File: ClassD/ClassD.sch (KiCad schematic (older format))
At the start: 1 part

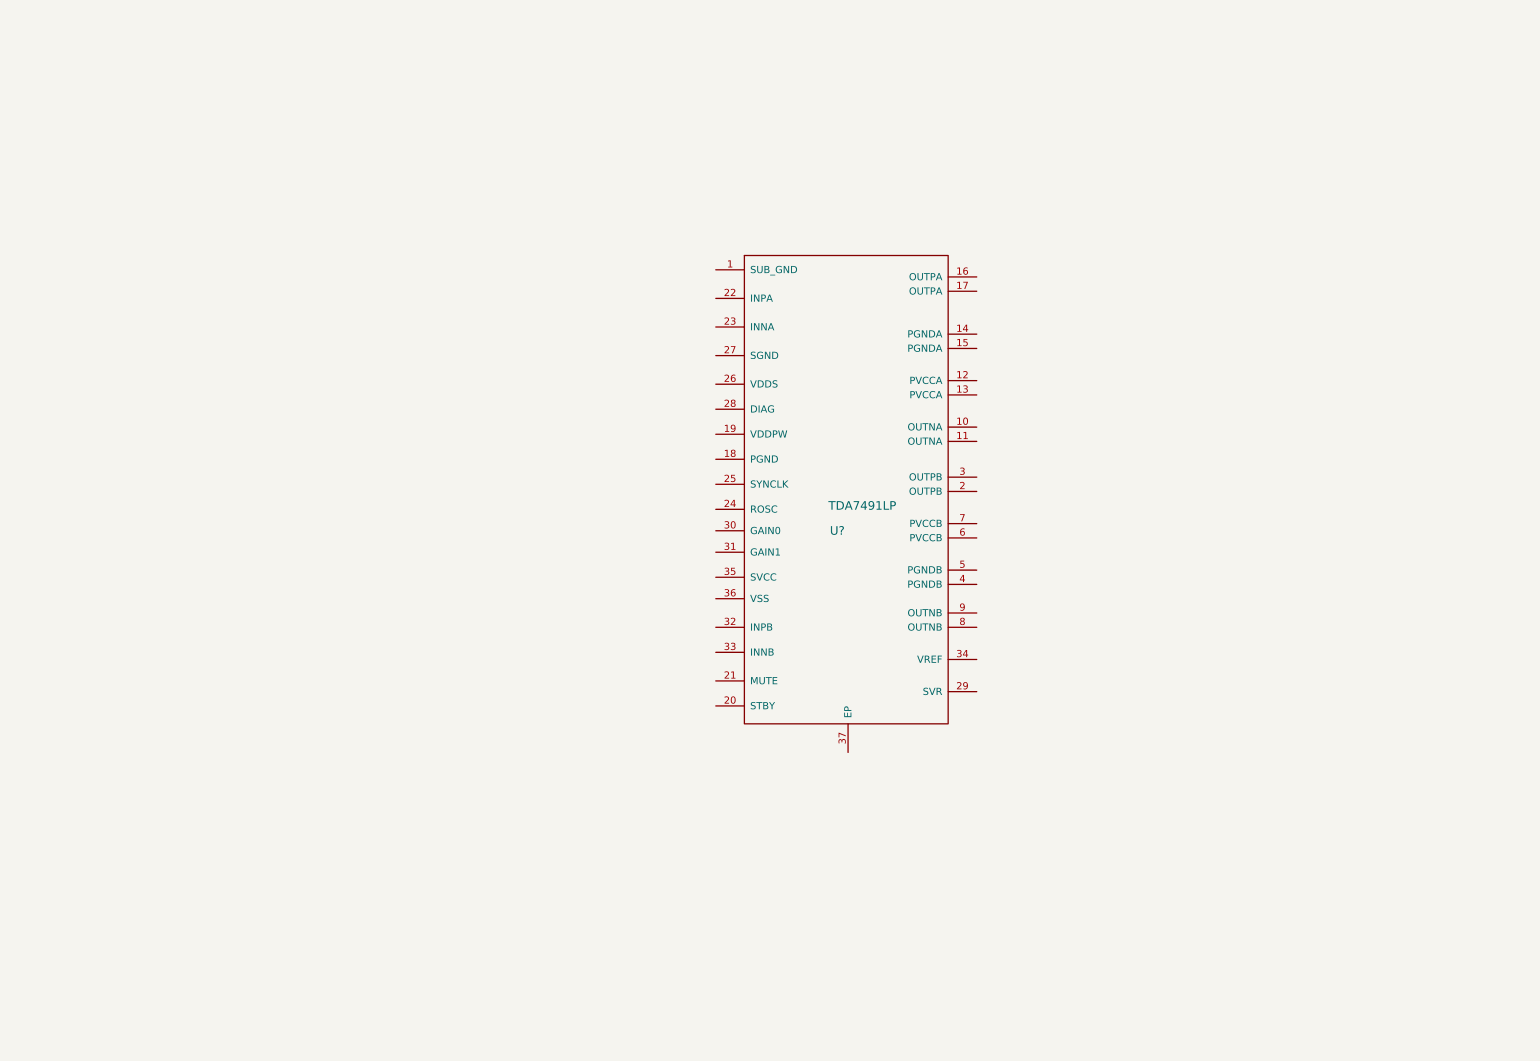
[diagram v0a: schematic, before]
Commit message: Created application schematic
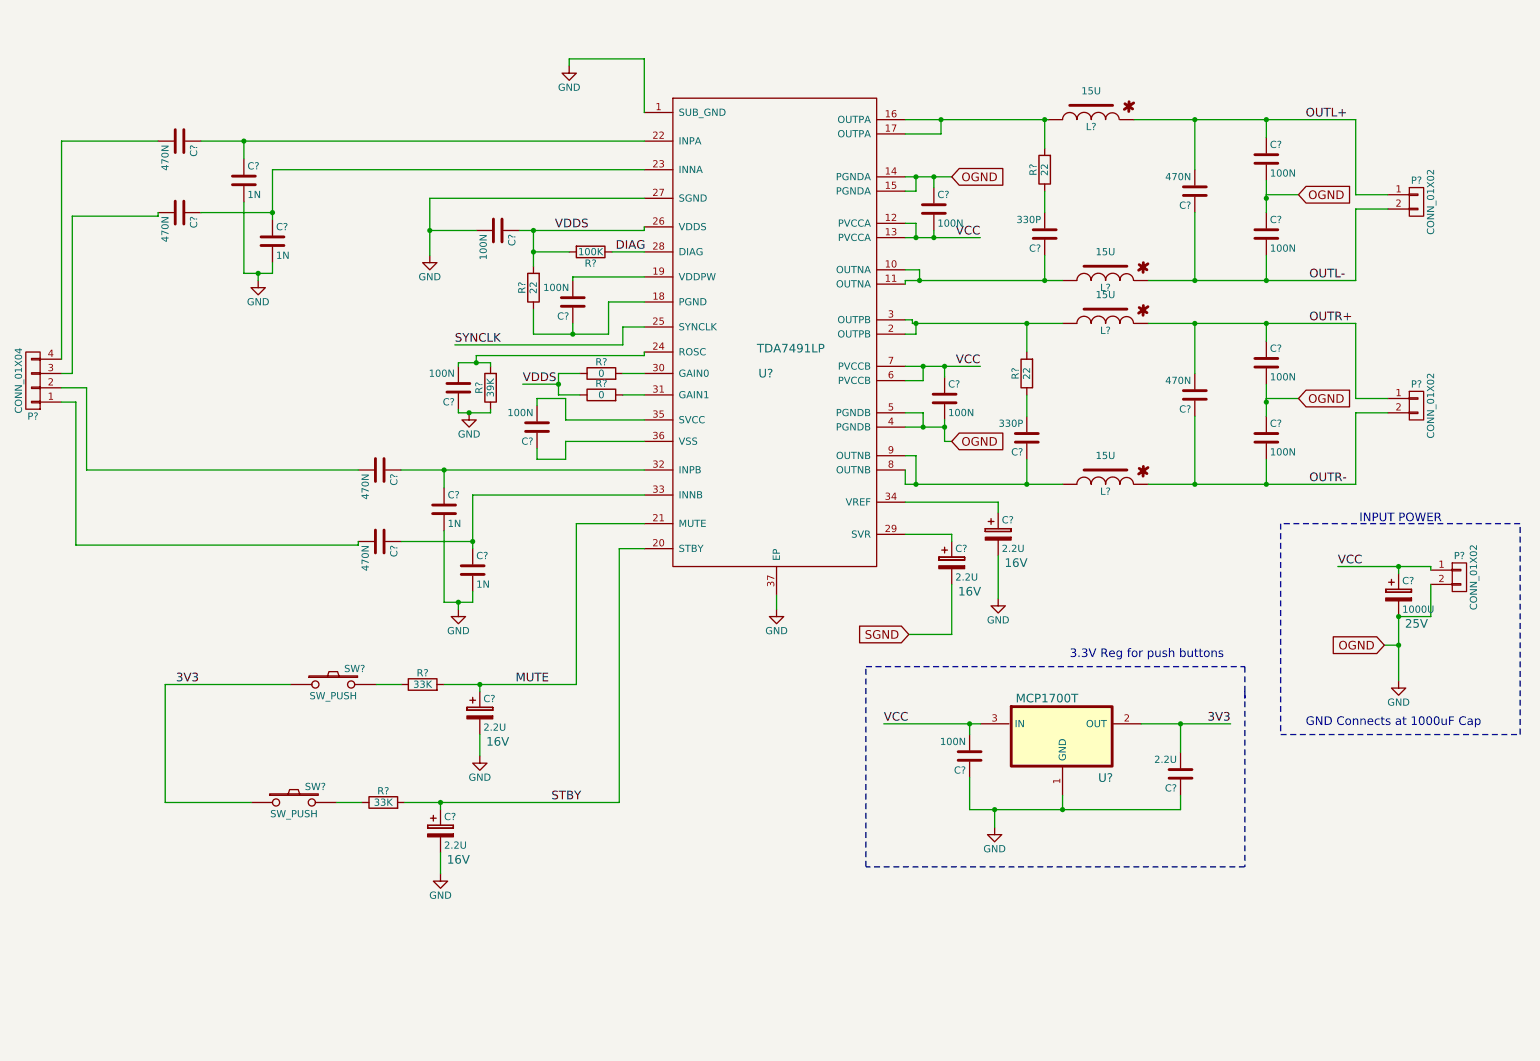
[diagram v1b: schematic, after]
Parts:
- removed U?: TDA7491LP, symbol TDA7491LP
- added C? (x4): 1N, symbol C
- added C? (x6): 470N, symbol C
- added C? (x11): 100N, symbol C
- added C? (x4): 2.2U, symbol CP
- added C?: 1000U, symbol CP
- added C? (x2): 330P, symbol C
- added C?: 2.2U, symbol C
- added L? (x4): 15U, symbol INDUCTOR-POL
- added P?: CONN_01X04, symbol CONN_01X04
- added P? (x3): CONN_01X02, symbol CONN_01X02
- added R?: 100K, symbol R
- added R? (x3): 22, symbol R
- added R?: 39K, symbol R
- added R? (x2): 0, symbol R
- added R? (x2): 33K, symbol R
- added SW? (x2): SW_PUSH, symbol SW_PUSH
- added U?: TDA7491LP, symbol TDA7491LP
- added U?: MCP1700T, symbol MCP1700T
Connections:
- new net: C?.1, L?.2, U?.10 (OUTNA), U?.11 (OUTNA)
- new net: L?.2, R?.2, U?.16 (OUTPA), U?.17 (OUTPA)
- new net: C?.1, R?.1, U?.18 (PGND)
- new net: C?.2, U?.19 (VDDPW)
- new net: L?.2, R?.2, U?.2 (OUTPB), U?.3 (OUTPB)
- new net: C?.1, C?.1, U?.22 (INPA)
- new net: C?.1, C?.1, U?.23 (INNA)
- new net: C?.2, R?.2, U?.24 (ROSC)
- new net: C?.1, U?.29 (SVR)
- new net: R?.2, U?.30 (GAIN0)
- new net: R?.2, U?.31 (GAIN1)
- new net: C?.1, C?.1, U?.32 (INPB)
- new net: C?.1, C?.1, U?.33 (INNB)
- new net: C?.1, U?.34 (VREF)
- new net: C?.2, U?.35 (SVCC)
- new net: C?.1, U?.36 (VSS)
- new net: C?.1, L?.2, U?.8 (OUTNB), U?.9 (OUTNB)
- new net: C?.2, P?.4 (P4)
- new net: C?.2, P?.3 (P3)
- new net: C?.2, P?.1 (P1)
- new net: C?.2, P?.2 (P2)
- new net: R?.1, SW?.2 (x2)
- new net: C?.2, R?.1 (x2)
- new net 3V3: C?.2, SW?.1, SW?.1, U?.2 (OUT)
- new net DIAG: R?.1, U?.28 (DIAG)
- new net GND: C?.1, C?.1, C?.1, C?.1, C?.1, C?.1, C?.2, C?.2, C?.2, C?.2, C?.2, C?.2, C?.2, C?.2, C?.2, C?.2, C?.2, C?.2, P?.2 (P2), R?.1, U?.1 (GND), U?.1 (SUB_GND), U?.14 (PGNDA), U?.15 (PGNDA), U?.27 (SGND), U?.37 (EP), U?.4 (PGNDB), U?.5 (PGNDB)
- new net MUTE: C?.1, R?.2, U?.21 (MUTE)
- new net OUTL+: C?.1, C?.2, L?.1, P?.1 (P1)
- new net OUTL-: C?.1, C?.2, L?.1, P?.2 (P2)
- new net OUTR+: C?.1, C?.2, L?.1, P?.1 (P1)
- new net OUTR-: C?.1, C?.2, L?.1, P?.2 (P2)
- new net SGND: C?.2
- new net STBY: C?.1, R?.2, U?.20 (STBY)
- new net SYNCLK: U?.25 (SYNCLK)
- new net VCC: C?.1, C?.1, C?.2, C?.2, P?.1 (P1), U?.12 (PVCCA), U?.13 (PVCCA), U?.3 (IN), U?.6 (PVCCB), U?.7 (PVCCB)
- new net VDDS: C?.1, R?.1, R?.1, R?.2, R?.2, U?.26 (VDDS)
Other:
- note added: "3.3V Reg for push buttons\n"
- note added: "GND Connects at 1000uF Cap"
- note added: "INPUT POWER"

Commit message: Updated schematic for ERC errors.
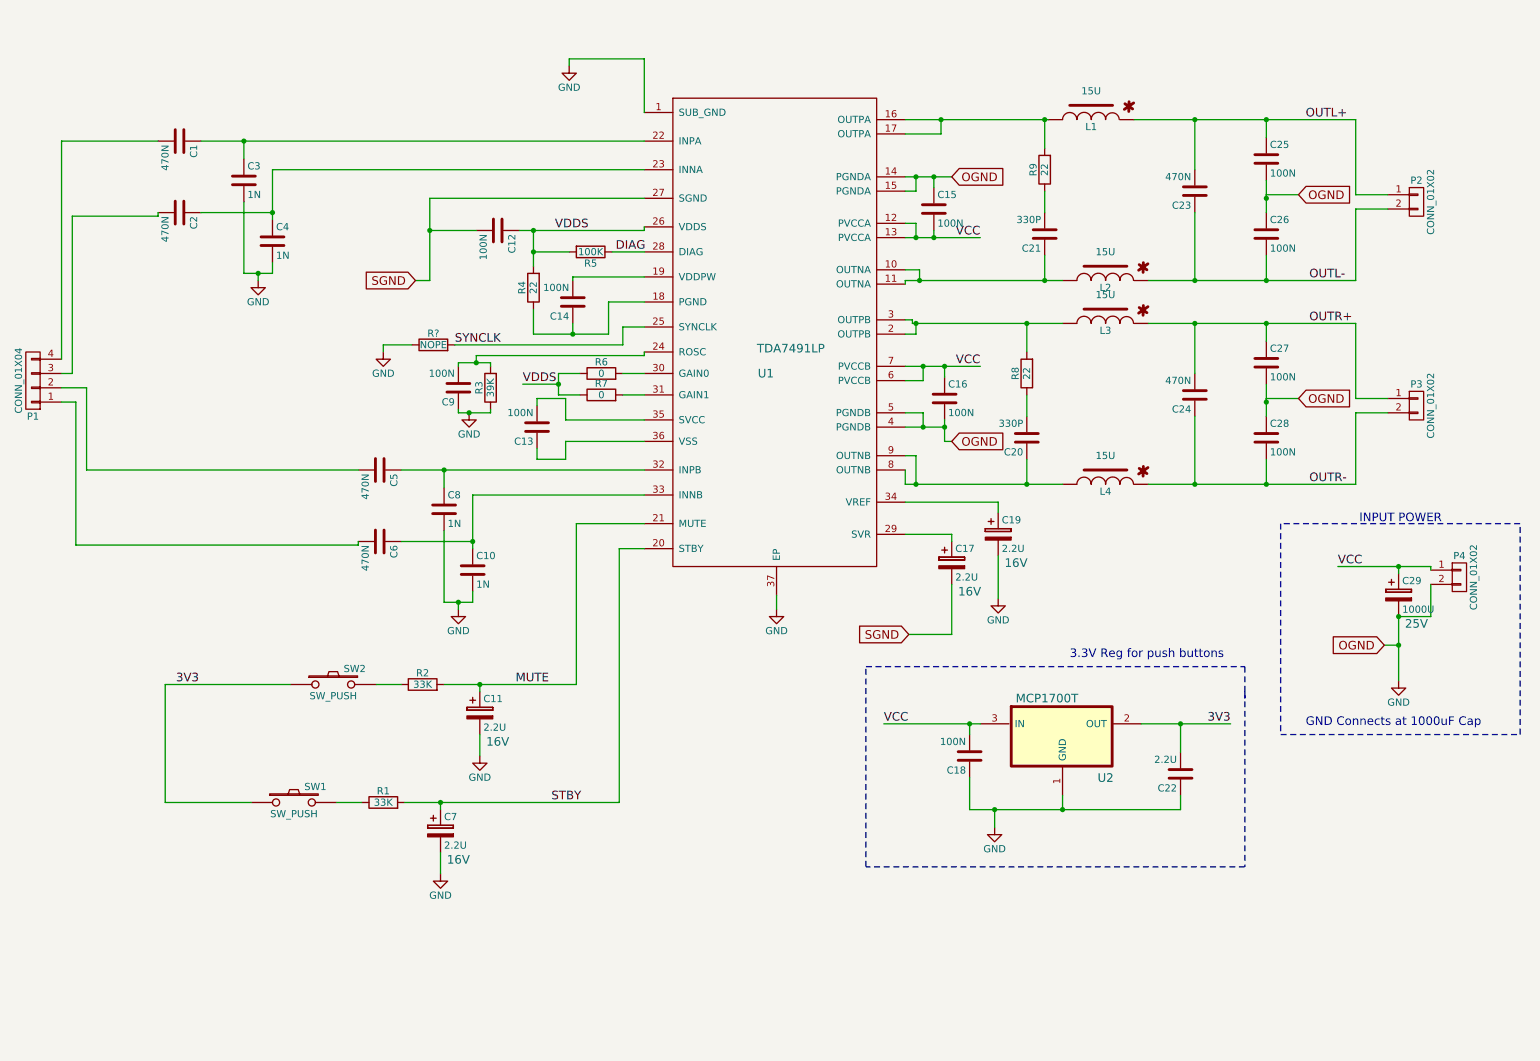
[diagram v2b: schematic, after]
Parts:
- removed U?: MCP1700T, symbol MCP1700T
- added R?: NOPE, symbol R
- added U2: MCP1700T, symbol MCP1700T
- gave numbers to parts that had none: 49
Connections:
- net 3V3: now also U2.2 (OUT)
- net GND: now also R?.1, U2.1 (GND); no longer C12.2, U1.27 (SGND)
- net SGND: now also C12.2, U1.27 (SGND)
- net SYNCLK: now also R?.2
- net VCC: now also U2.3 (IN)

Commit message: Added critical component MPNs to the schematic
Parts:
- removed C1, C2, C24, C5, C6: 470N, symbol C
- removed C11, C17, C19, C7: 2.2U, symbol CP
- removed L1, L2, L4: 15U, symbol INDUCTOR-POL
- removed SW1: SW_PUSH, symbol SW_PUSH
- added C? (x4): 2.2U, 1206, symbol CP
- added C? (x5): 470N, 1206, symbol C
- added L? (x3): 15U, symbol INDUCTOR-POL
- added SW?: SW_PUSH, symbol SW_PUSH
- C23: footprint (none) -> 1206; Link (none) -> http://www.digikey.com/product-detail/en/CL31B474KAFNNNE/12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; MPN (none) -> CL31B474KAFNNNE; Voltage (none) -> 25
- C25: footprint (none) -> 0805; Link (none) -> http://www.digikey.com/product-detail/en/C0805C104K4RACTU/3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; MPN (none) -> C0805C104K4RACTU; Voltage (none) -> 16
- C29: Link (none) -> http://www.digikey.com/product-detail/en/UUG1E102MNQ1MS/493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; MPN (none) -> UUG1E102MNQ1MS
- C3: footprint (none) -> 0805; Link (none) -> http://www.digikey.com/product-detail/en/C0805C102K5RACTU/3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; MPN (none) -> C0805C102K5RACTU
- L3: Link (none) -> http://www.digikey.com/product-detail/en/NRS6045T150MMGK/58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; MPN (none) -> NRS6045T150MMGK
- SW2: Link (none) -> http://www.digikey.com/product-detail/en/FSM2JSMAA/FSM2JSMA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; MPN (none) -> FSM2JSMAA
- U1: Link (none) -> http://www.digikey.com/product-detail/en/TDA7491LP13TR/497-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; MPN (none) -> TDA7491LP13TR
- U2: Link (none) -> http://www.digikey.com/product-detail/en/MCP1700T-3302E%2FT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; MPN (none) -> MCP1700T-3302E/TT; Voltage (none) -> 3.3
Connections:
- net 3V3: now also SW?.1
- net GND: now also C?.2, C?.2, C?.2
- net MUTE: now also C?.1
- net OUTL+: now also L?.1
- net OUTL-: now also L?.1
- net OUTR+: now also C?.2
- net OUTR-: now also C?.1, L?.1
- net SGND: now also C?.2
- net STBY: now also C?.1
- net at C21.1, U1.10 (OUTNA), U1.11 (OUTNA): now also L?.2
- net at R9.2, U1.16 (OUTPA), U1.17 (OUTPA): now also L?.2
- net at C3.1, U1.22 (INPA): now also C?.2
- net at C4.1, U1.23 (INNA): now also C?.2
- net at U1.29 (SVR): now also C?.1
- net at C8.1, U1.32 (INPB): now also C?.2
- net at C10.1, U1.33 (INNB): now also C?.2
- net at U1.34 (VREF): now also C?.1
- net at C20.1, U1.8 (OUTNB), U1.9 (OUTNB): now also L?.2
- net at P1.4 (P4): now also C?.1
- net at P1.3 (P3): now also C?.1
- net at P1.1 (P1): now also C?.1
- net at P1.2 (P2): now also C?.1
- net at R1.1: now also SW?.2

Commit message: Created and associated all footprints
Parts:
- removed P1: CONN_01X04, symbol CONN_01X04
- added P1: RedRCA, ClassD:RCJ1x, symbol CONN_01X02
- added P2: WhiteRCA, ClassD:RCJ1x, symbol CONN_01X02
- C1: renamed from C?; footprint 1206 -> Capacitors_SMD:C_1206_HandSoldering
- C10, C12, C13, C14, C15, C16, C18, C26, C27, C28, C4, C8, C9: footprint (none) -> Capacitors_SMD:C_0805
- C11, C17, C19, C2, C24, C5, C6: renamed from C?; footprint 1206 -> Capacitors_SMD:C_1206
- C20, C21: footprint (none) -> Capacitors_SMD:C_0805; Link (none) -> http://www.digikey.com/product-detail/en/0805YC334KAT2A/478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; MPN (none) -> 0805YC334KAT2A
- C22: footprint (none) -> Capacitors_SMD:C_1206
- C23: footprint 1206 -> Capacitors_SMD:C_1206
- C25, C3: footprint 0805 -> Capacitors_SMD:C_0805
- C29: footprint (none) -> ClassD:c_elec_13.6x13.6
- C7: renamed from C?; footprint 1206 -> Capacitors_SMD:c_elec_5x5.3
- L1, L2, L4: renamed from L?; footprint (none) -> ClassD:NRS6045T150MMGK
- L3: footprint (none) -> ClassD:NRS6045T150MMGK
- P3: renamed from P2; footprint (none) -> Pin_Headers:Pin_Header_Straight_1x02
- P4: renamed from P3; footprint (none) -> Pin_Headers:Pin_Header_Straight_1x02
- P5: renamed from P4; footprint (none) -> Pin_Headers:Pin_Header_Straight_1x02
- R1, R2: footprint (none) -> Resistors_SMD:R_0805
- R10: renamed from R9; footprint (none) -> Resistors_SMD:R_0805
- R3: renamed from R?; footprint (none) -> Resistors_SMD:R_0805
- R4: renamed from R3; footprint (none) -> Resistors_SMD:R_0805
- R5: renamed from R4; footprint (none) -> Resistors_SMD:R_0805
- R6: renamed from R5; footprint (none) -> Resistors_SMD:R_0805
- R7: renamed from R6; footprint (none) -> Resistors_SMD:R_0805
- R8: renamed from R7; footprint (none) -> Resistors_SMD:R_0805
- R9: renamed from R8; footprint (none) -> Resistors_SMD:R_0805
- gave numbers to parts that had none: 1
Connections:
- net at C6.1: now also P2.1 (P1)
- net at C5.1: now also P2.2 (P2)
- net at C2.1: now also P1.1 (P1)
- net at C1.1: now also P1.2 (P2)

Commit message: Updated footprint names in schematic
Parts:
- SW1, SW2: footprint (none) -> ClassD:FSM2JSMAA-ND
- U2: footprint (none) -> TO_SOT_Packages_SMD:SOT-23
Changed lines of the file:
@@
 F 0 "SW2" H 2850 5285 50  0000 C CNN
 F 1 "SW_PUSH" H 2700 5095 50  0000 C CNN
-F 2 "" H 2700 5175 50  0001 C CNN
+F 2 "ClassD:FSM2JSMAA-ND" H 2700 5175 50  0001 C CNN
 F 3 "" H 2700 5175 50  0000 C CNN
 F 4 "http://www.digikey.com/product-detail/en/FSM2JSMAA/FSM2JSMAA-ND/2400228" H 2700 5175 60  0001 C CNN "Link"
@@
 F 0 "U2" H 8101 5072 60  0000 C CNN
 F 1 "MCP1700T" H 7691 5628 60  0000 C CNN
-F 2 "" H 8070 6065 60  0001 C CNN
+F 2 "TO_SOT_Packages_SMD:SOT-23" H 8070 6065 60  0001 C CNN
 F 3 "" H 8070 6065 60  0000 C CNN
 F 4 "http://www.digikey.com/product-detail/en/MCP1700T-3302E%2FTT/MCP1700T3302ETTCT-ND/652677" H 7800 5450 60  0001 C CNN "Link"
@@
 F 0 "SW1" H 2575 6110 50  0000 C CNN
 F 1 "SW_PUSH" H 2425 5920 50  0000 C CNN
-F 2 "" H 2425 6000 50  0001 C CNN
+F 2 "ClassD:FSM2JSMAA-ND" H 2425 6000 50  0001 C CNN
 F 3 "" H 2425 6000 50  0000 C CNN
 F 4 "http://www.digikey.com/product-detail/en/FSM2JSMAA/FSM2JSMAA-ND/2400228" H 2425 6000 60  0001 C CNN "Link"

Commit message: Added power indicator LED
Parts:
- added D1: LED, LEDs:LED_0805, symbol LED
- added R11: 499, Resistors_SMD:R_0805, symbol R
- C7: footprint Capacitors_SMD:c_elec_5x5.3 -> Capacitors_SMD:C_1206
- U1: footprint (none) -> ClassD:PowerSSO36-EPD
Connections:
- net 3V3: now also D1.2 (A)
- net GND: now also R11.2
- new net: D1.1 (K), R11.1
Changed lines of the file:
@@
 F 0 "U1" H 5725 2750 60  0000 C CNN
 F 1 "TDA7491LP" H 5900 2925 60  0000 C CNN
-F 2 "" H 5875 3650 60  0001 C CNN
+F 2 "ClassD:PowerSSO36-EPD" H 5875 3650 60  0001 C CNN
 F 3 "" H 5875 3650 60  0000 C CNN
 F 4 "http://www.digikey.com/product-detail/en/TDA7491LP13TR/497-11056-1-ND/2571081" H 5800 2875 60  0001 C CNN "Link"
@@
 F 0 "C7" H 3475 6300 50  0000 L CNN
 F 1 "2.2U" H 3475 6100 50  0000 L CNN
-F 2 "Capacitors_SMD:c_elec_5x5.3" H 3488 6050 50  0000 C CNN
+F 2 "Capacitors_SMD:C_1206" H 3488 6050 50  0000 C CNN
 F 3 "" H 3450 6200 50  0000 C CNN
 F 4 "http://www.digikey.com/product-detail/en/C3216X7R1E225K160AA/445-1382-1-ND/567633" H 3450 6200 60  0001 C CNN "Link"
@@
 	-1   0    0    1
 $EndComp
+$Comp
+L LED D1
+U 1 1 56CB515D
+P 8875 5800
+F 0 "D1" H 8875 5900 50  0000 C CNN
+F 1 "LED" H 8875 5700 50  0000 C CNN
+F 2 "LEDs:LED_0805" H 8875 5800 50  0001 C CNN
+F 3 "" H 8875 5800 50  0000 C CNN
+	1    8875 5800
+	0    -1   -1   0
+$EndComp
+Wire Wire Line
+	8875 5600 8875 5450
+Connection ~ 8875 5450
+$Comp
+L R R11
+U 1 1 56CB538B
+P 8600 6250
+F 0 "R11" V 8680 6250 50  0000 C CNN
+F 1 "499" V 8600 6250 50  0000 C CNN
+F 2 "Resistors_SMD:R_0805" V 8530 6250 50  0000 C CNN
+F 3 "" H 8600 6250 50  0000 C CNN
+	1    8600 6250
+	0    1    1    0
+$EndComp
+Wire Wire Line
+	8875 6000 8875 6250
+Wire Wire Line
+	8875 6250 8750 6250
+Wire Wire Line
+	8450 6250 8200 6250
+Wire Wire Line
+	8200 6250 8200 6050
+Connection ~ 8200 6050
 $EndSCHEMATC
